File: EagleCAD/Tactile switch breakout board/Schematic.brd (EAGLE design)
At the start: 18.5 x 21.5 mm, 2 parts

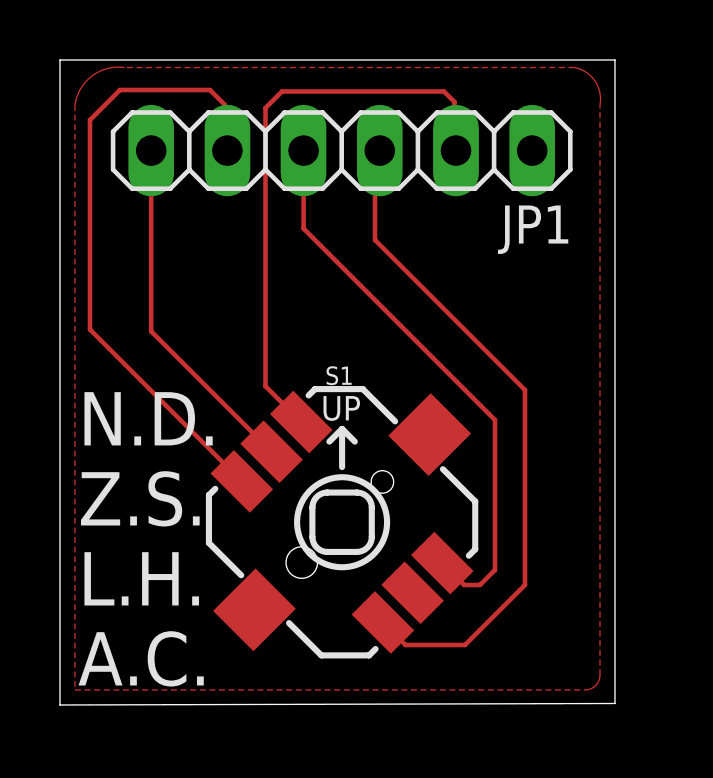
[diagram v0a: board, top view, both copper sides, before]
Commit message: Modded switch breakout board, sent design away. Also added OSHPark design rules file
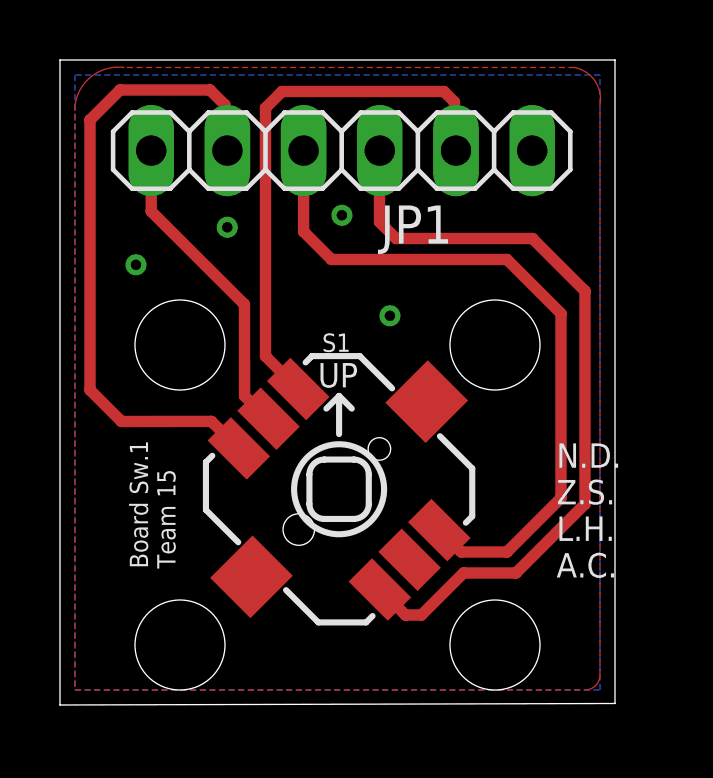
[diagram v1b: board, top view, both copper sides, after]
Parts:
- moved S1 1.10 mm to (9.30, 7.19)
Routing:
- net N$1: track 18.9 -> 23.7 mm
- net N$7: track 22.5 -> 26.0 mm
- net N$8: track 19.3 -> 18.1 mm
- net N$2: track 11.7 -> 10.6 mm
- net N$3: track 20.8 -> 21.4 mm
- added copper zone on layer 16, net GND
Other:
- board text added: "Board Sw.1 Team 15"
